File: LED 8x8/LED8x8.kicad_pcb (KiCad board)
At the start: 2 copper layers, 226.1 x 251.5 mm, 214 parts, among them J101 Conn_01x05_Male, Q201 2N3906, Q202 2N3906, Q203 2N3906, Q204 2N3906, Q205 2N3906, Q206 2N3906, Q207 2N3906, Q208 2N3906, Q209 2N3904, Q210 2N3904, Q211 2N3904, Q212 2N3904, Q213 2N3904, Q214 2N3904, Q215 2N3904, Q216 2N3904, Q301 2N3904, SW301 SW_SPST, U101 4024, U102 4081, U201 74HCT138, U301 74HC00, U302 NE555P, U303 4024, U304 NE555P, U401 74HCT574, U402 74HCT574, U403 74HCT574, U404 74HCT574, U405 74HCT574, U406 74HCT574, U407 74HCT574, U408 74HCT574, U409 74HCT138, U501 74LS138, U502 74HCT540, U601 74HC164, U602 74HC164

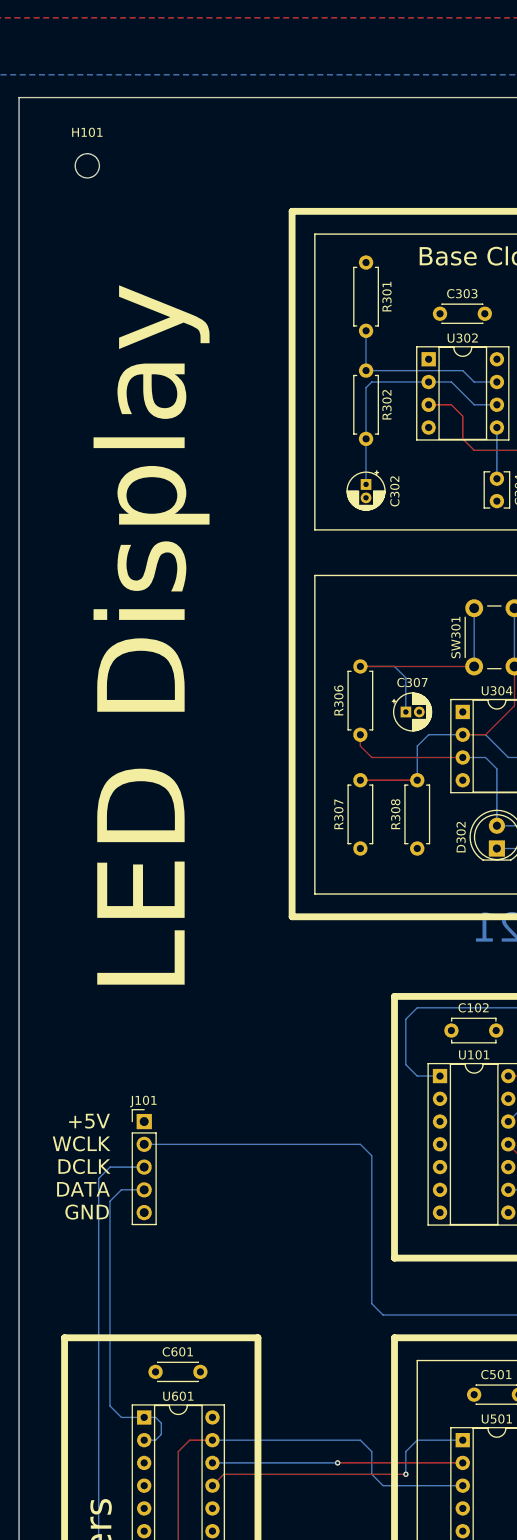
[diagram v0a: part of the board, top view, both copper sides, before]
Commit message: Had address register connected backwards on LED 8x8
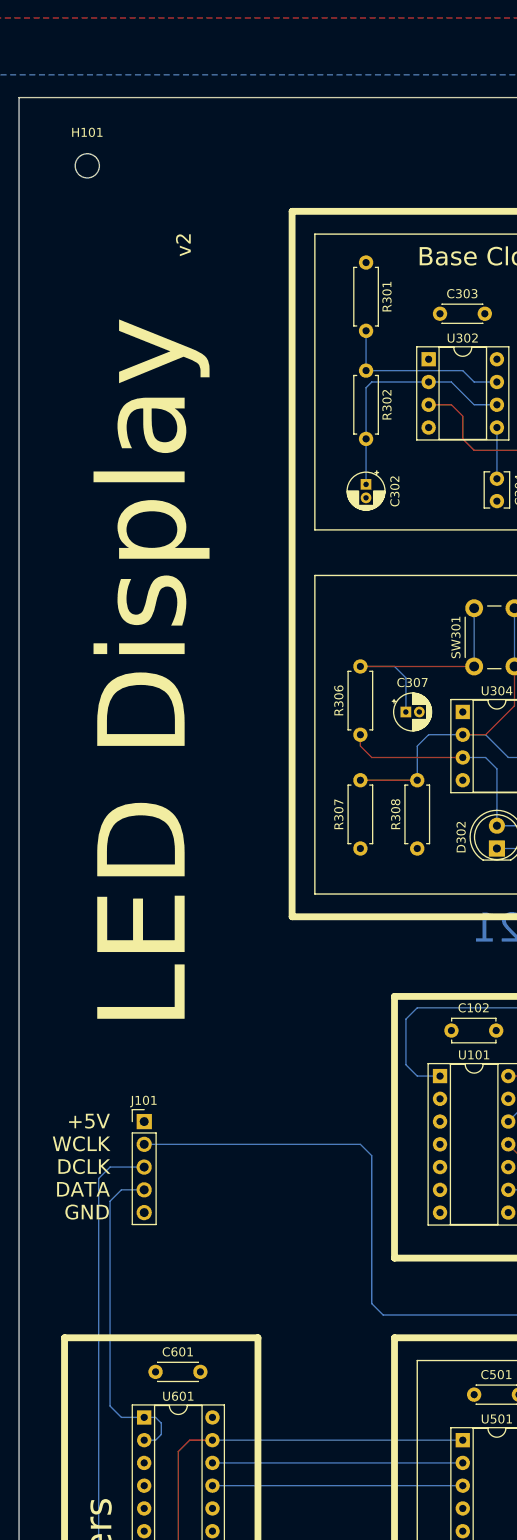
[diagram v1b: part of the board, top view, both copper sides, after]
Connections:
- U601 pad 11: /Input Registers/Addr0 -> /Input Registers/Addr2
- U601 pad 13: /Input Registers/Addr2 -> /Input Registers/Addr0
- U602 pad 1: /Input Registers/Addr2 -> /Input Registers/Addr0
- U602 pad 2: /Input Registers/Addr2 -> /Input Registers/Addr0
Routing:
- net /Input Registers/Addr2: track 79.9 -> 27.9 mm
- net /Input Registers/Addr0: track 31.5 -> 76.3 mm, vias 1 -> 0
- net /Input Registers/Addr1: vias 1 -> 0
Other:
- board text added: "v2"
